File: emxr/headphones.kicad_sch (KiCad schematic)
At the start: 39 parts, among them IC301 NJM4556D

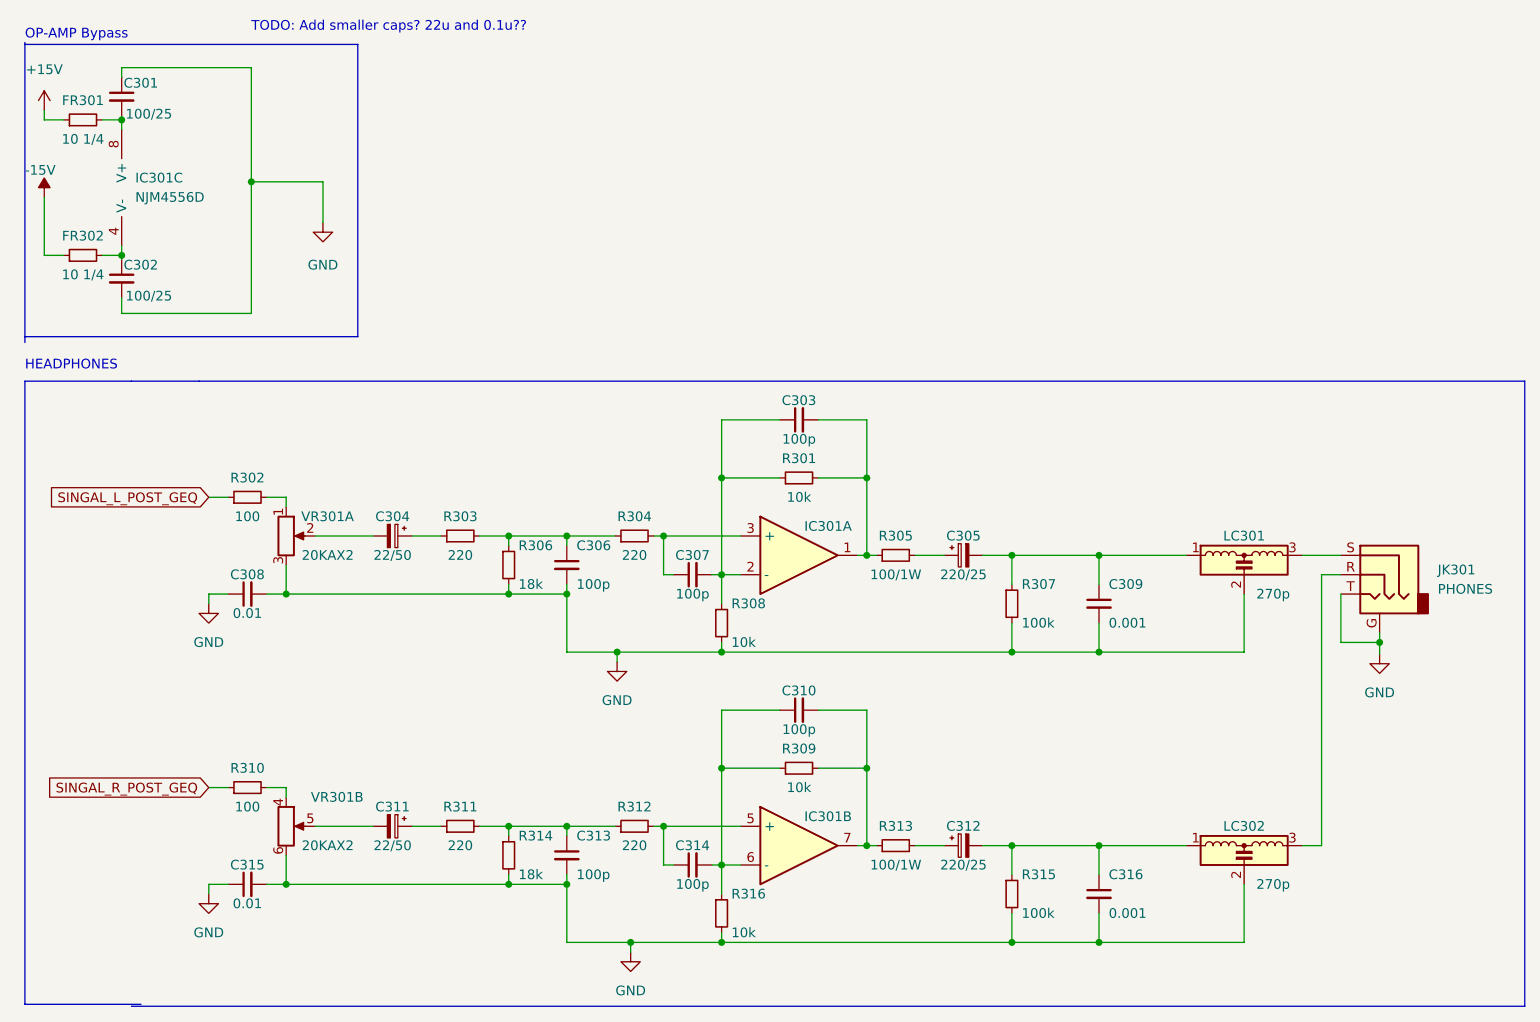
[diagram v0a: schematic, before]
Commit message: finish footprints, starting on component placement
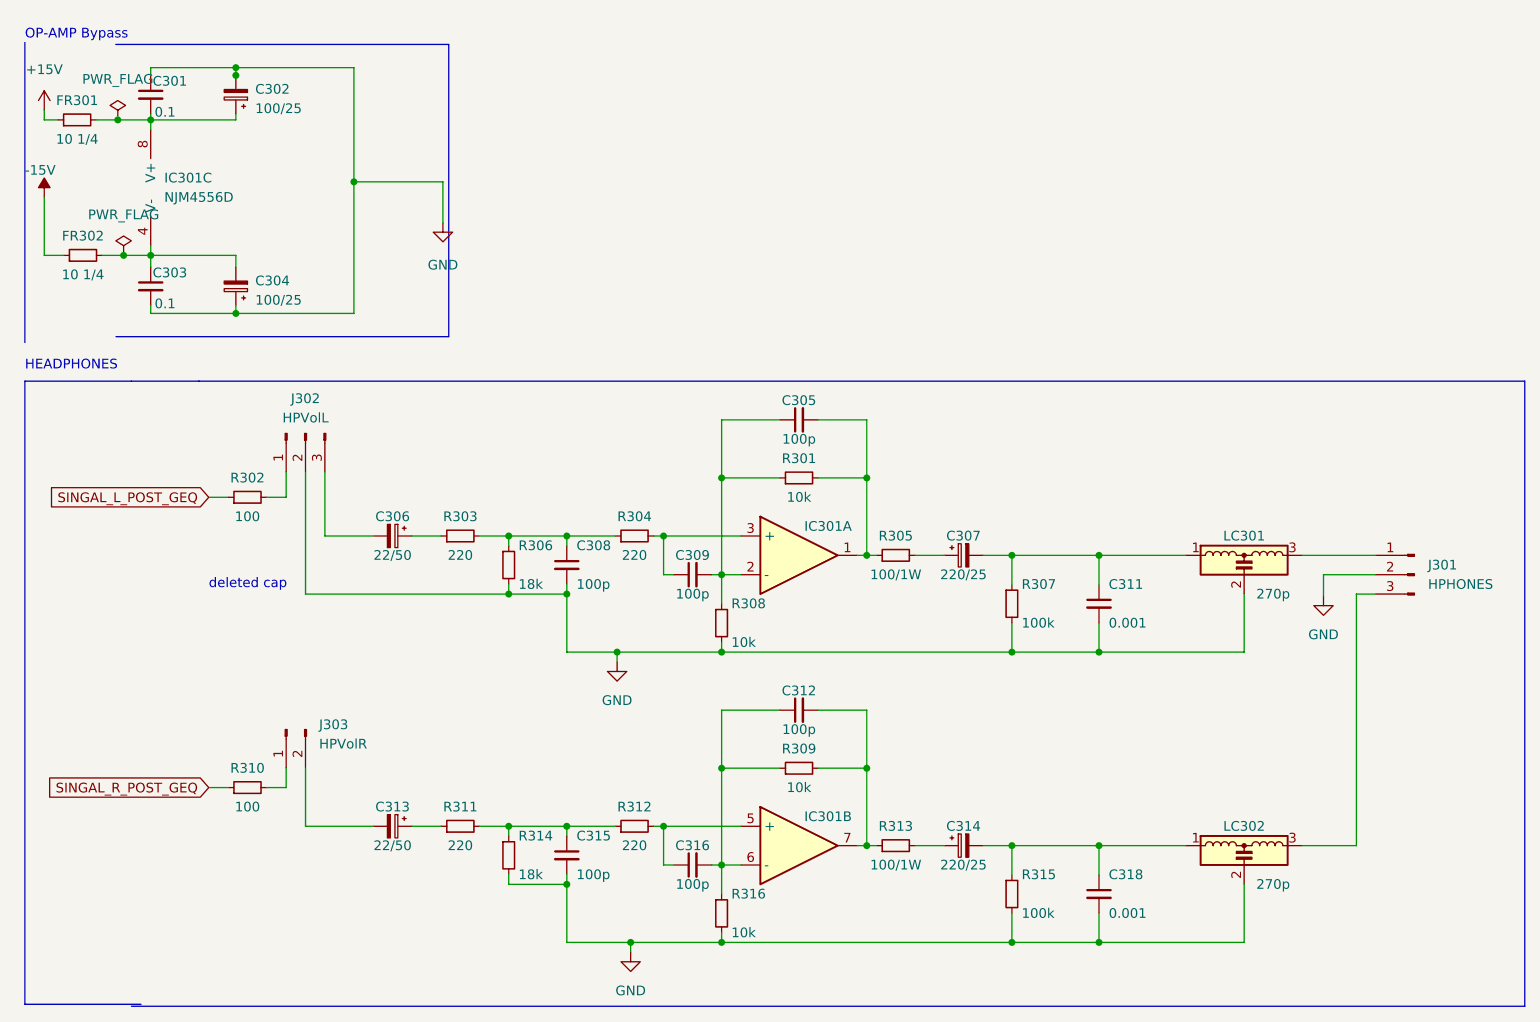
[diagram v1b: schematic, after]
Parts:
- removed C308, C315: 0.01, symbol Device:C_Small
- removed JK301: PHONES, symbol Connector:AudioJack3_Ground
- removed VR301: 20KAX2, symbol Device:R_Potentiometer_Dual_Separate
- added C302, C304: 100/25, Capacitor_THT:CP_Radial_D8.0mm_P3.50mm, symbol Device:C_Polarized_Small
- added J301: HPHONES, Connector_JST:JST_XH_B3B-XH-A_1x03_P2.50mm_Vertical, symbol Connector:Conn_01x03_Male
- added J302: HPVolL, Connector_JST:JST_XH_B3B-XH-A_1x03_P2.50mm_Vertical, symbol Connector:Conn_01x03_Male
- added J303: HPVolR, Connector_JST:JST_XH_B2B-XH-A_1x02_P2.50mm_Vertical, symbol Connector:Conn_01x02_Male
- C301: value 100/25 -> 0.1; footprint (none) -> Capacitor_THT:C_Disc_D3.8mm_W2.6mm_P2.50mm
- C303: renamed from C302; value 100/25 -> 0.1; footprint (none) -> Capacitor_THT:C_Disc_D3.8mm_W2.6mm_P2.50mm
- C305: renamed from C303; footprint (none) -> Capacitor_THT:C_Disc_D5.0mm_W2.5mm_P2.50mm
- C306: renamed from C304; footprint (none) -> Capacitor_THT:CP_Radial_D5.0mm_P2.00mm
- C307: renamed from C305; footprint (none) -> Capacitor_THT:CP_Radial_D10.0mm_P5.00mm
- C308: renamed from C306; footprint (none) -> Capacitor_THT:C_Disc_D5.0mm_W2.5mm_P2.50mm
- C309: renamed from C307; footprint (none) -> Capacitor_THT:C_Disc_D5.0mm_W2.5mm_P2.50mm
- C311: renamed from C309; footprint (none) -> Capacitor_THT:C_Disc_D3.8mm_W2.6mm_P2.50mm
- C312: renamed from C310; footprint (none) -> Capacitor_THT:C_Disc_D5.0mm_W2.5mm_P2.50mm
- C313: renamed from C311; footprint (none) -> Capacitor_THT:CP_Radial_D5.0mm_P2.00mm
- C314: renamed from C312; footprint (none) -> Capacitor_THT:CP_Radial_D10.0mm_P5.00mm
- C315: renamed from C313; footprint (none) -> Capacitor_THT:C_Disc_D5.0mm_W2.5mm_P2.50mm
- C316: renamed from C314; footprint (none) -> Capacitor_THT:C_Disc_D5.0mm_W2.5mm_P2.50mm
- C318: renamed from C316; footprint (none) -> Capacitor_THT:C_Disc_D3.8mm_W2.6mm_P2.50mm
- FR301, FR302: footprint (none) -> Resistor_THT:R_Axial_DIN0207_L6.3mm_D2.5mm_P5.08mm_Vertical
- IC301: footprint (none) -> Package_DIP:DIP-8_W7.62mm_Socket_LongPads
- LC301, LC302: footprint (none) -> dba_footprint:LCL_EMX
- R301, R302, R303, R304, R306, R307, R308, R309, R310, R311, R312, R314, R315, R316: footprint (none) -> Resistor_THT:R_Axial_DIN0207_L6.3mm_D2.5mm_P10.16mm_Horizontal
- R305, R313: footprint (none) -> Resistor_THT:R_Axial_DIN0207_L6.3mm_D2.5mm_P15.24mm_Horizontal
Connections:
- net GND: now also C302.2, C304.1, J301.2 (Pin_2), J302.2 (Pin_2)
- net at R302.2: now also J302.1 (Pin_1)
- net at R310.2: now also J303.1 (Pin_1)
- net at LC302.3: now also J301.3 (Pin_3)
- net at LC301.3: now also J301.1 (Pin_1)
- net at C306.2: now also J302.3 (Pin_3)
- net at C303.1, FR302.2, IC301.4 (V-): now also C304.2
- net at C301.2, FR301.2, IC301.8 (V+): now also C302.1
- net at C313.2: now also J303.2 (Pin_2)
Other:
- note added: "deleted cap"
- note removed: "TODO: Add smaller caps? 22u and 0.1u??"
- moved on the sheet: C301, C303, FR301, IC301C

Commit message: first pcb draft
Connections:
- net at R310.2: now also J303.2 (Pin_2); no longer J303.1 (Pin_1)
- net at C313.2: now also J303.1 (Pin_1); no longer J303.2 (Pin_2)
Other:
- moved on the sheet: J303
